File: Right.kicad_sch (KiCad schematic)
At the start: 32 parts, among them J2 Conn_01x02, J4 10103594-0001LF, U2 W25Q128JVS, U3 RP2040, U9 LM1117-3.3, Y1 ECS-120-8-33-JGN-TR3

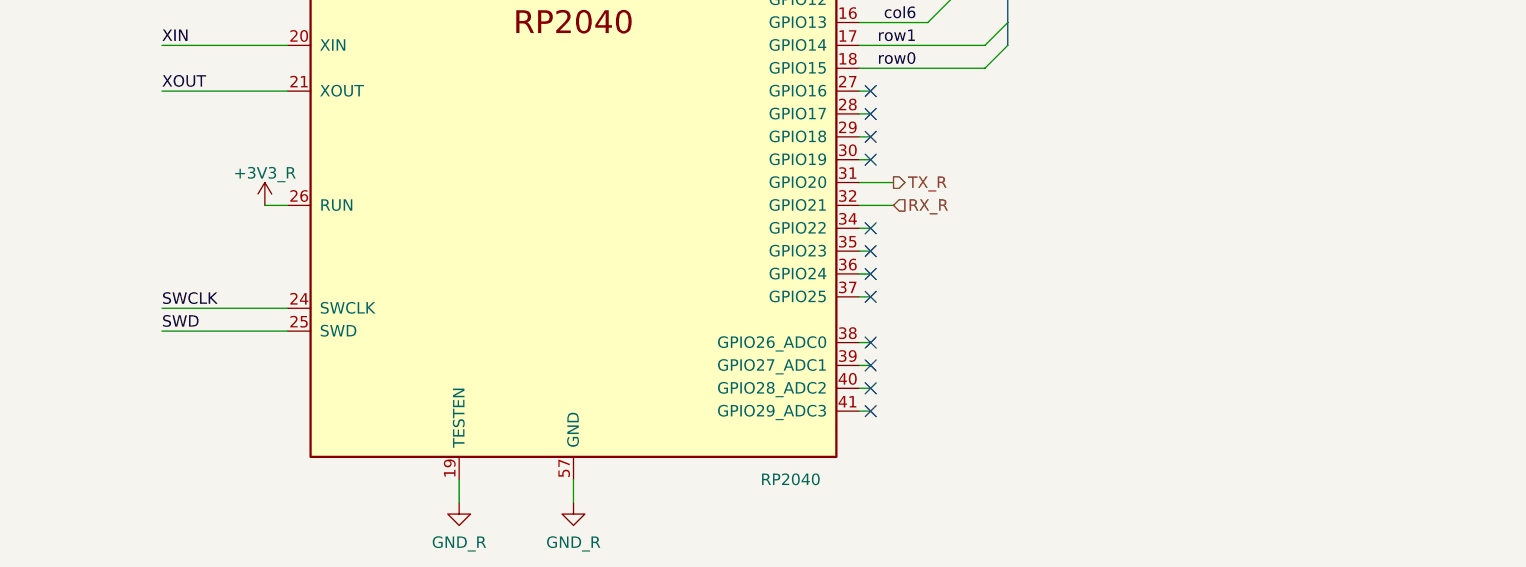
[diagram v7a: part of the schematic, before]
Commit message: Left side case created in blender
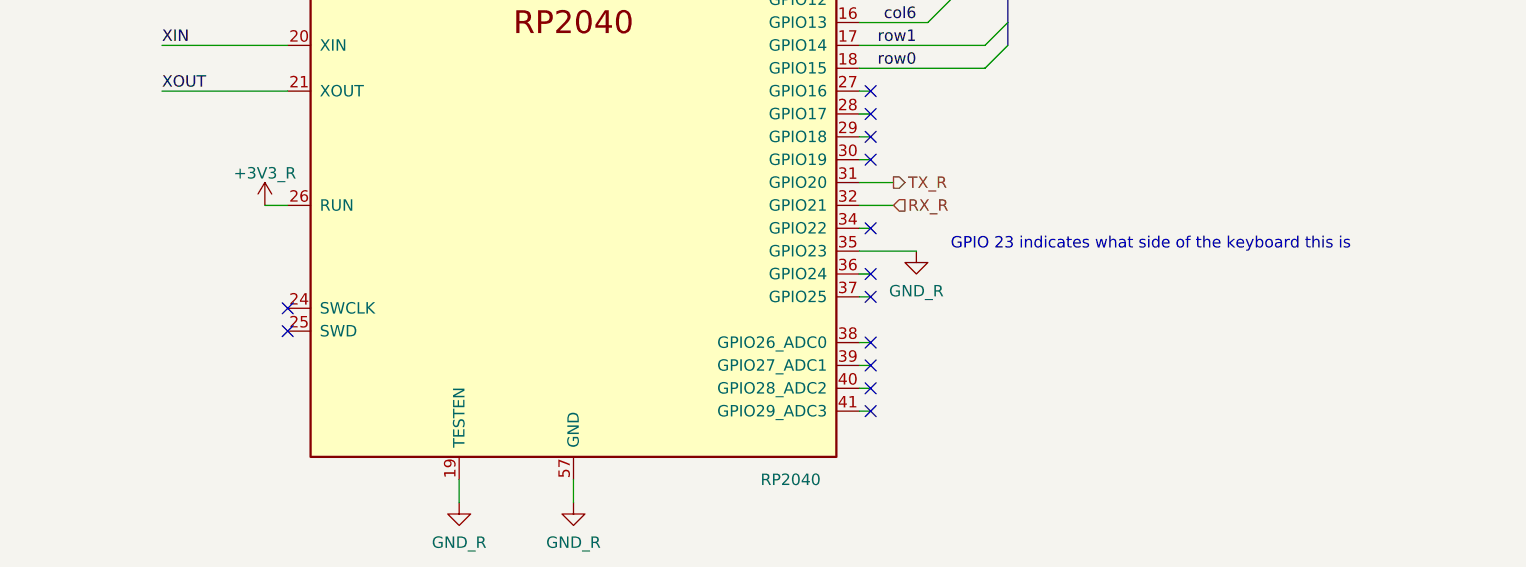
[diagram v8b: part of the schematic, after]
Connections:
- net GND_R: now also U3.35 (GPIO23)
- net SWCLK: no longer names the net of U3.24 (SWCLK)
- net SWD: no longer names the net of U3.25 (SWD)
- no-connect marks 18 -> 19
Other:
- note added: "GPIO 23 indicates what side of the keyboard this is"
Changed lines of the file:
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@@
   (no_connect (at 201.93 152.4))
   (no_connect (at 201.93 149.86))
-  (no_connect (at 201.93 137.16))
+  (no_connect (at 137.16 146.05))
   (no_connect (at 201.93 154.94))
   (no_connect (at 201.93 139.7))
   (no_connect (at 201.93 127))
   (no_connect (at 201.93 142.24))
+  (no_connect (at 137.16 143.51))
   (no_connect (at 31.75 35.56))
   (no_connect (at 200.66 86.36))
@@
     (stroke (width 0) (type default) (color 0 0 0 0))
   )
-  (wire (pts (xy 201.93 137.16) (xy 200.66 137.16))
+  (wire (pts (xy 200.66 137.16) (xy 207.01 137.16))
     (stroke (width 0) (type default) (color 0 0 0 0))
   )
@@
     (stroke (width 0) (type default) (color 0 0 0 0))
   )
-  (wire (pts (xy 137.16 143.51) (xy 123.19 143.51))
-    (stroke (width 0) (type default) (color 0 0 0 0))
-  )
   (wire (pts (xy 73.66 114.3) (xy 73.66 115.57))
     (stroke (width 0) (type default) (color 0 0 0 0))
@@
   )
   (wire (pts (xy 217.17 36.83) (xy 217.17 39.37))
-    (stroke (width 0) (type default) (color 0 0 0 0))
-  )
-  (wire (pts (xy 137.16 146.05) (xy 123.19 146.05))
     (stroke (width 0) (type default) (color 0 0 0 0))
   )
@@
     (effects (font (size 1.27 1.27)) (justify left bottom))
   )
+  (text "GPIO 23 indicates what side of the keyboard this is"
+    (at 210.82 137.16 0)
+    (effects (font (size 1.27 1.27)) (justify left bottom))
+  )
   (text "Crystal" (at 39.37 142.24 0)
     (effects (font (size 2.54 2.54)) (justify left bottom))
@@
     (effects (font (size 1.27 1.27)) (justify right bottom))
   )
-  (label "SWD" (at 123.19 146.05 0)
-    (effects (font (size 1.27 1.27)) (justify left bottom))
-  )
   (label "col0" (at 207.01 88.9 180)
     (effects (font (size 1.27 1.27)) (justify right bottom))
@@
   (label "row4" (at 207.01 78.74 180)
     (effects (font (size 1.27 1.27)) (justify right bottom))
-  )
-  (label "SWCLK" (at 123.19 143.51 0)
-    (effects (font (size 1.27 1.27)) (justify left bottom))
   )
   (label "col3" (at 207.01 101.6 180)
@@
     (pin "2")
   )
+  (symbol (lib_id "arisu-split:GND_R") (at 207.01 137.16 0) (unit 1)
+    (in_bom yes) (on_board yes) (fields_autoplaced)
+    (property "Reference" "#PWR0166" (id 0) (at 207.01 143.51 0)
+      (effects (font (size 1.27 1.27)) hide)
+    )
+    (property "Value" "GND_R" (id 1) (at 207.01 141.6034 0))
+    (property "Footprint" "" (id 2) (at 207.01 137.16 0)
+      (effects (font (size 1.27 1.27)) hide)
+    )
+    (property "Datasheet" "" (id 3) (at 207.01 137.16 0)
+      (effects (font (size 1.27 1.27)) hide)
+    )
+    (pin "1")
+  )
   (symbol (lib_id "arisu-split:GND_R") (at 50.8 158.75 0) (unit 1)
